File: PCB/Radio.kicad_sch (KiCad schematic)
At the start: 25 parts, among them J501 Conn_Coaxial, U501 SX1262IMLTRT, U502 SKY13453-385LF, Y501 32 MHz

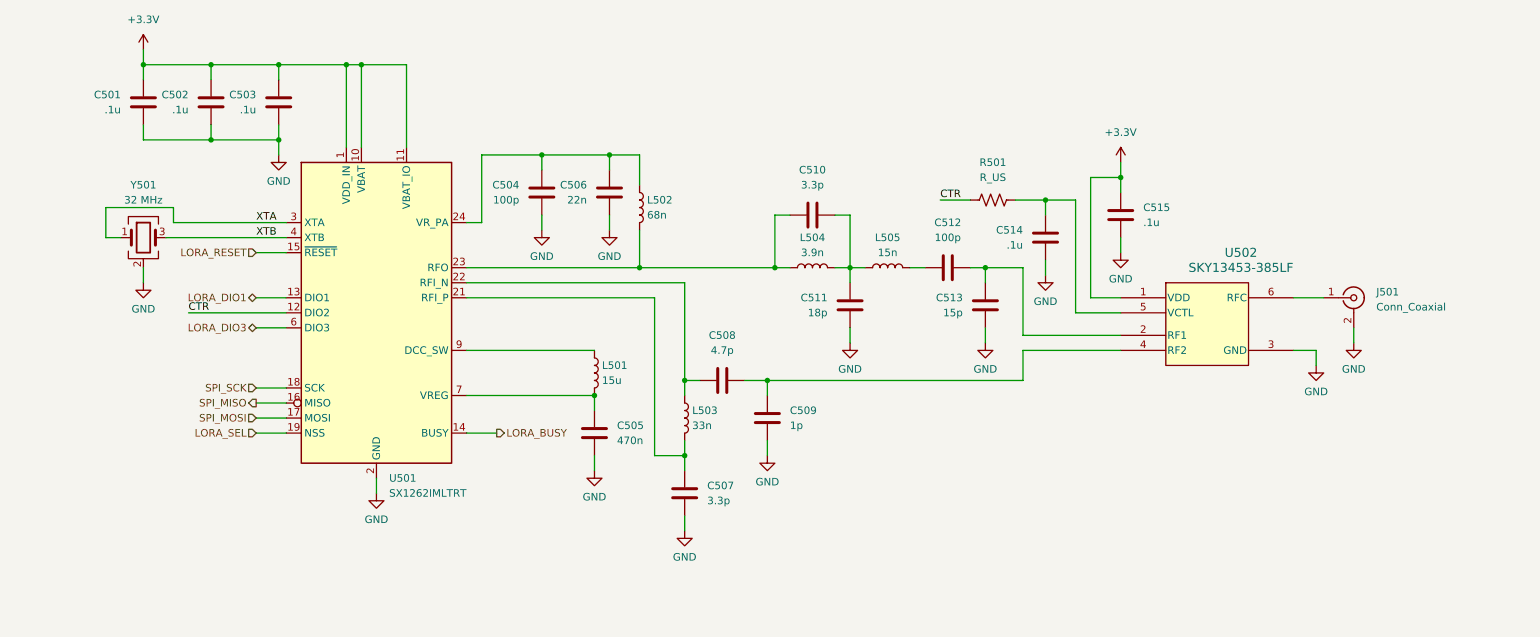
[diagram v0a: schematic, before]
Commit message: Updated PCB to have the new parts (unrouted)
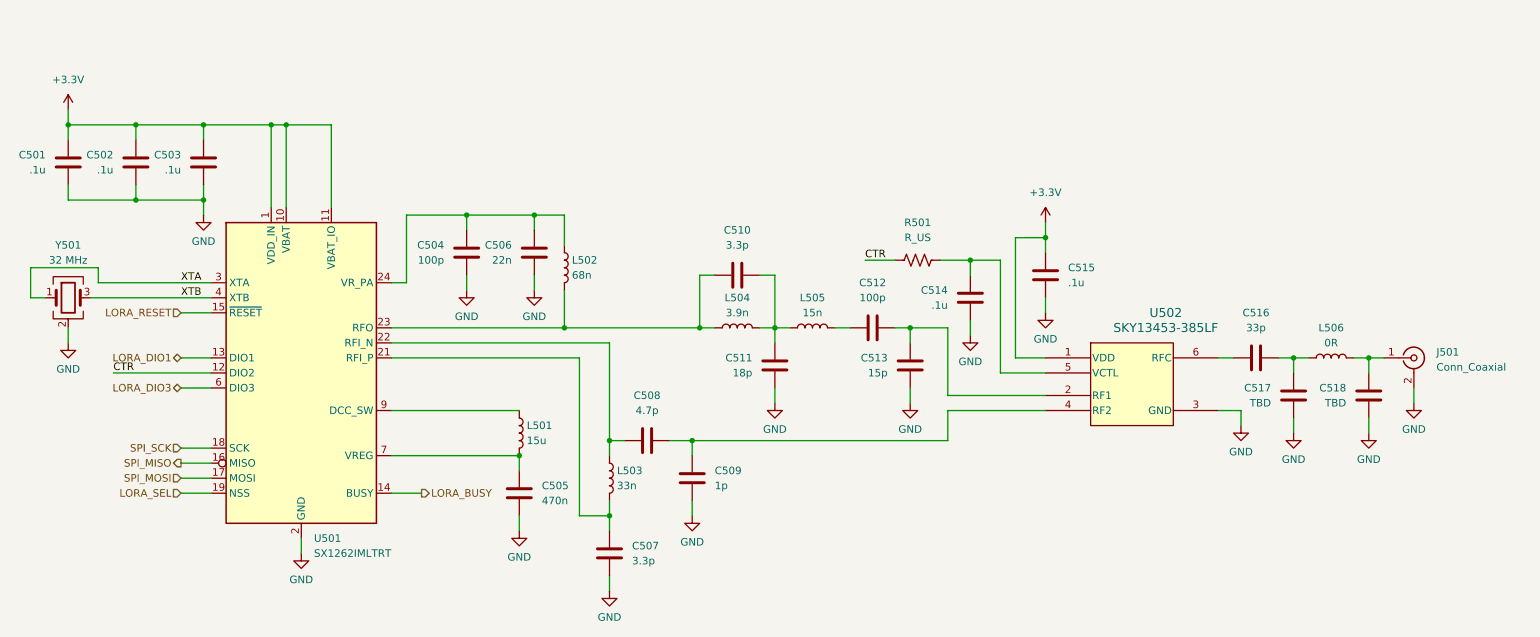
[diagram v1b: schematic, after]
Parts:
- added C516: 33p, Capacitor_SMD:C_0603_1608Metric_Pad1.08x0.95mm_HandSolder, symbol Device:C
- added C517, C518: TBD, Capacitor_SMD:C_0603_1608Metric_Pad1.08x0.95mm_HandSolder, symbol Device:C
- added L506: 0R, Inductor_SMD:L_0603_1608Metric_Pad1.05x0.95mm_HandSolder, symbol Device:L
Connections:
- net GND: now also C517.2, C518.2
- net at U502.6 (RFC): now also C516.1; no longer J501.1 (In)
- new net: C516.2, C517.1, L506.1
- new net: C518.1, J501.1 (In), L506.2
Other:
- moved on the sheet: C501, C502, C503, C504, C505, C506, C507, C508, C509, C510, C511, C512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

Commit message: Updated BOM
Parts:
- R501: value R_US -> 500
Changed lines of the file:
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@@
 			)
 		)
-		(property "Value" "R_US"
+		(property "Value" "500"
 			(at 173.99 77.47 90)
 			(show_name no)

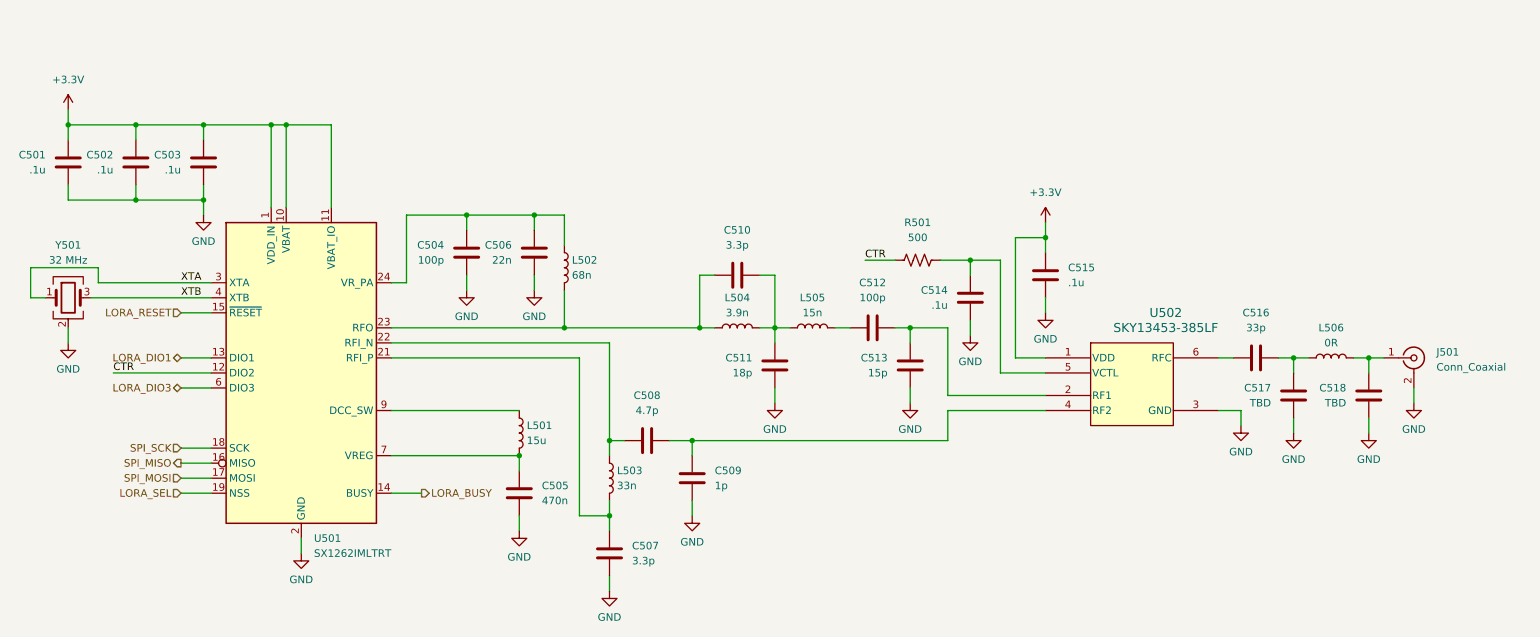
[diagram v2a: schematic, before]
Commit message: - Renamed all NETs connected to MCU sheet to the pin name - Cleaned up schematic - Named all unnamed NETs
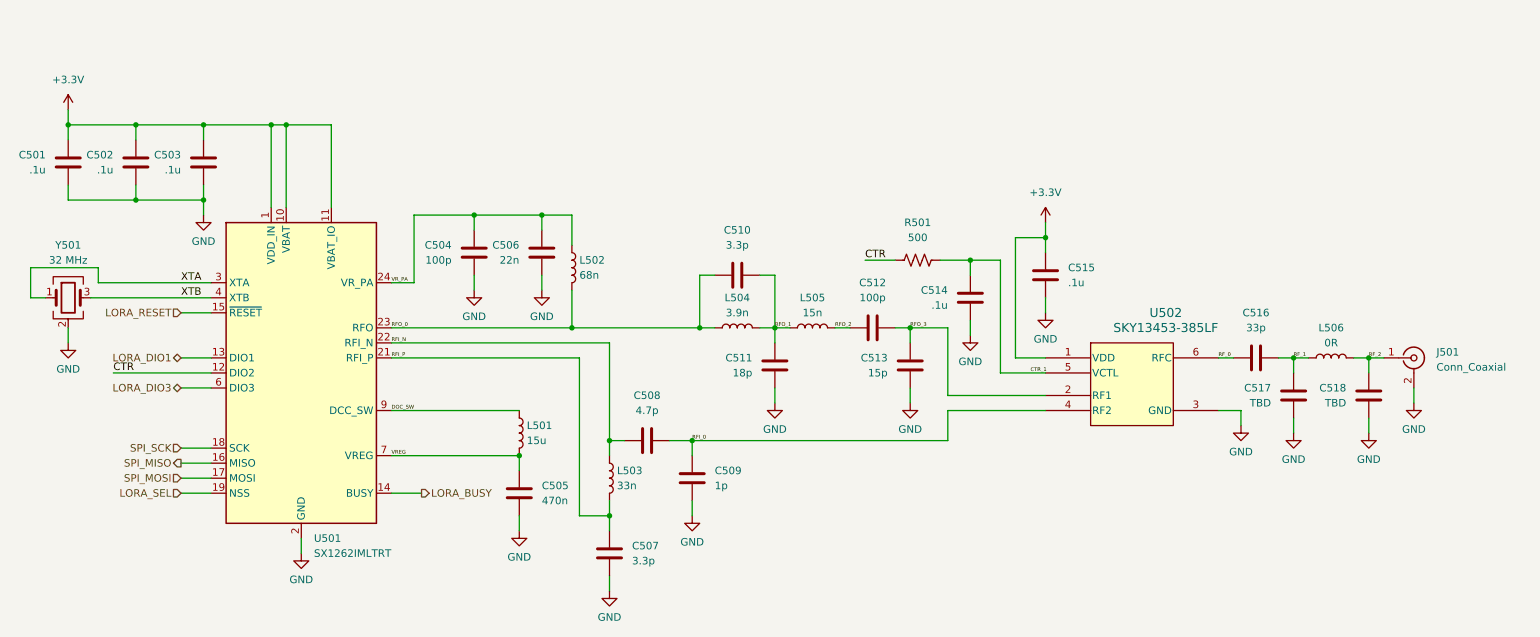
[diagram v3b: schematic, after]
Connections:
- net RFI_P: now reaches C507.1, L503.2, U501.21 (RFI_P)
- net RFI_N: now reaches C508.2, L503.1, U501.22 (RFI_N)
- net RFO_0: now reaches C510.1, L502.2, L504.1, U501.23 (RFO)
- net VR_PA: now reaches C504.1, C506.1, L502.1, U501.24 (VR_PA)
- net VREG: now reaches C505.1, L501.2, U501.7 (VREG)
- net DOC_SW: now reaches L501.1, U501.9 (DCC_SW)
- net RF_1: now reaches C516.2, C517.1, L506.1
- net RF_0: now reaches C516.1, U502.6 (RFC)
- net RFO_2: now reaches C512.2, L505.1
- net RFO_1: now reaches C510.2, C511.1, L504.2, L505.2
- net CTR_1: now reaches C514.1, R501.2, U502.5 (VCTL)
- net RFI_0: now reaches C508.1, C509.1, U502.4 (RF2)
- net RF_2: now reaches C518.1, J501.1 (In), L506.2
- net RFO_3: now reaches C512.1, C513.1, U502.2 (RF1)
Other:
- moved on the sheet: C504, C506, L502
